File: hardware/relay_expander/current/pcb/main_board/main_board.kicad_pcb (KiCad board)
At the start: 2 copper layers, 100 x 85 mm, 101 parts, among them J1 Conn_01x07_Socket, J10 Screw_Terminal_01x02, J11 Screw_Terminal_01x02, J12 Screw_Terminal_01x02, J13 Screw_Terminal_01x02, J14 Screw_Terminal_01x02, J15 Screw_Terminal_01x02, J16 Conn_01x20_Socket, J2 Conn_01x07_Socket, J3 Screw_Terminal_01x02, J4 Screw_Terminal_01x02, J5 Screw_Terminal_01x02, J6 Screw_Terminal_01x02, J7 Screw_Terminal_01x02, J8 Screw_Terminal_01x03, J9 Screw_Terminal_01x02, K1 HF46F-12-HS1, K2 HF46F-12-HS1, K3 HF46F-12-HS1, K4 HF46F-12-HS1, K5 HF46F-12-HS1, K6 HF46F-12-HS1, K7 HF46F-12-HS1, K8 HF46F-12-HS1, Q1 BC548, Q2 BC548, Q3 BC548, Q4 BC548, Q5 BC548, Q6 BC548, Q7 BC548, Q8 BC548, SW1 SW_DIP_x03, U1 MCP23017x-x-SO, U2 TCMT4100, U3 TCMT4100, U4 TCMT4100, U5 TCMT4100

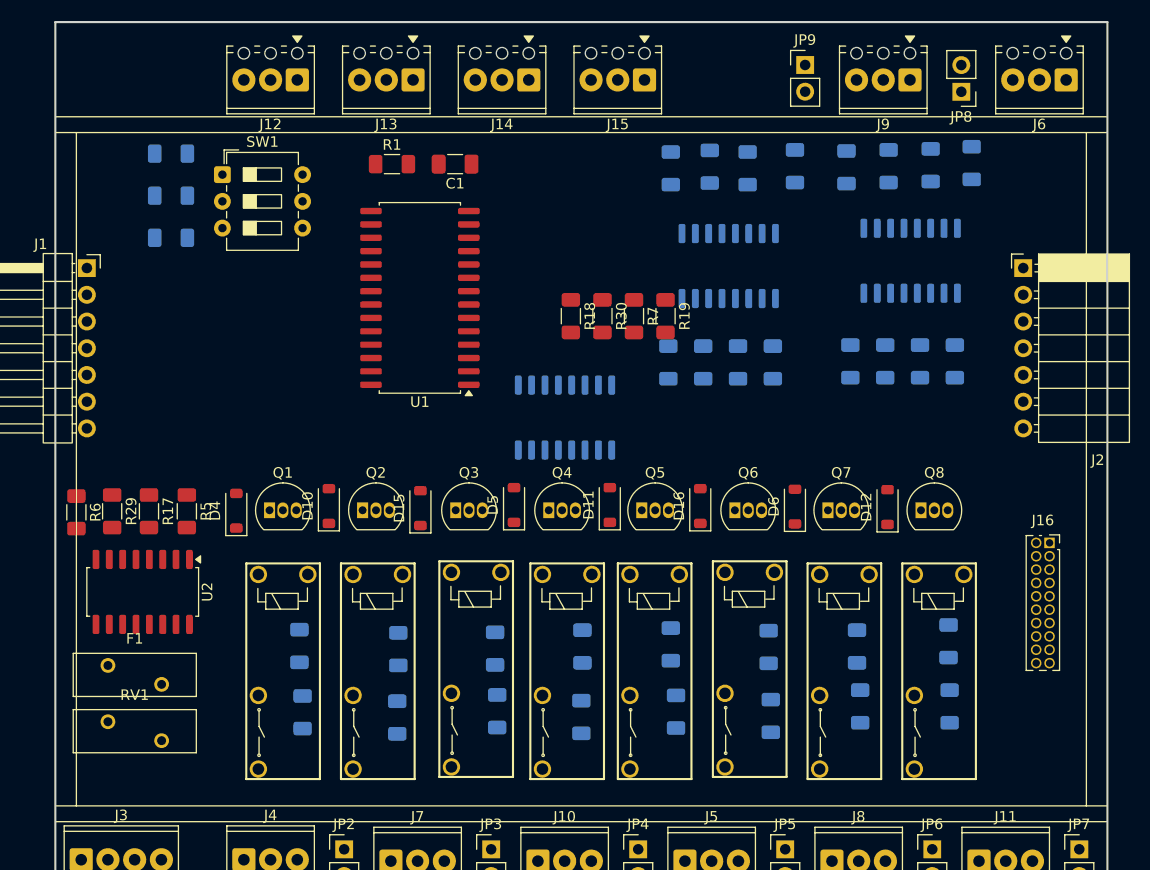
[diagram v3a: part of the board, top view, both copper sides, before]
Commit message: [FIX] placement of connector for UI panel
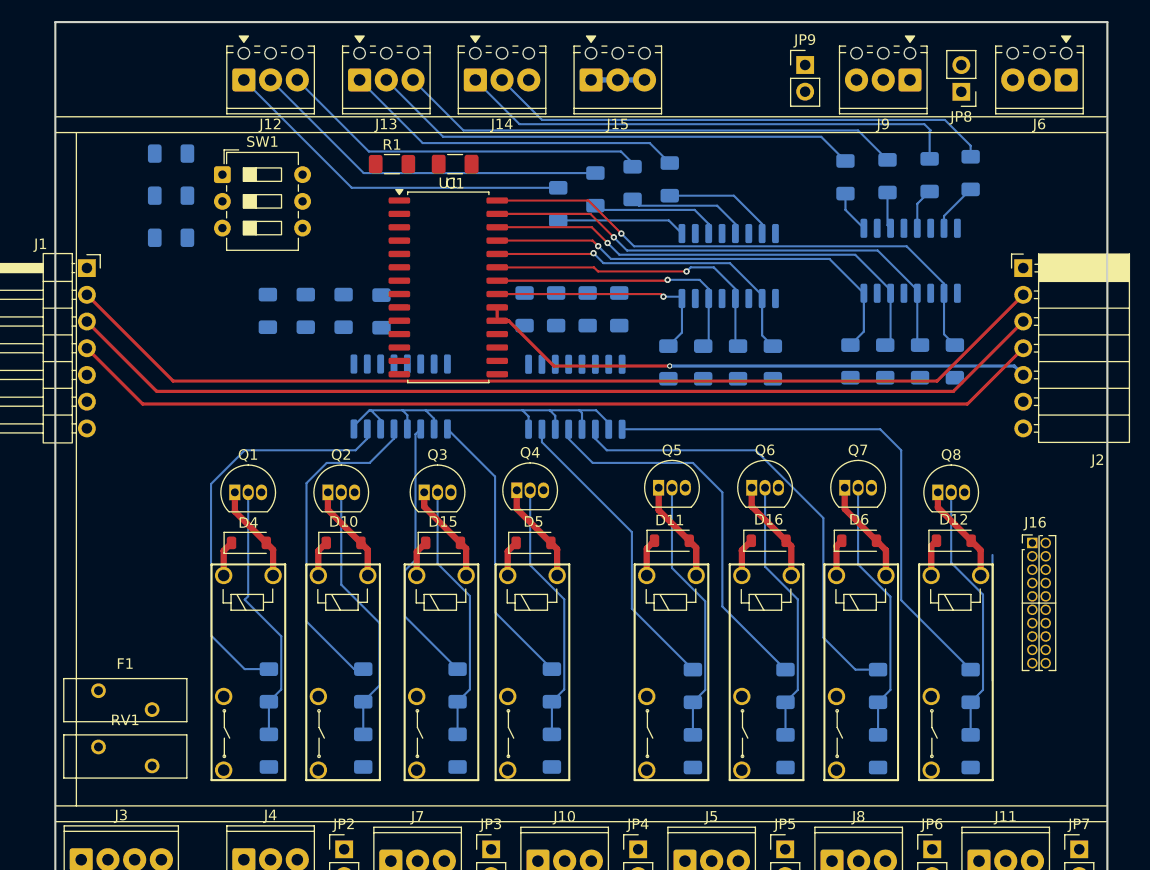
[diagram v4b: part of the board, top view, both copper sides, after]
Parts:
- J16: footprint Connector_PinSocket_1.27mm:PinSocket_2x10_P1.27mm_Vertical -> homeautomation_core:PinSocket_2x10_P1.27mm_Vertical
- R17, R18, R19, R29, R30, R5, R6, R7, U2: moved to B.Cu
- moved R6 34.7 mm to (116.0, 80.0)
- moved U2 30.8 mm to (117.8, 88.1)
- moved R29 29.1 mm to (112.4, 80.0)
- moved R17 24.2 mm to (108.8, 80.0)
- moved R5 20.5 mm to (105.2, 80.0)
- moved R40 12.0 mm to (143.4, 67.5)
- moved R37 11.2 mm to (132.8, 69.8)
- moved R38 11.1 mm to (136.3, 68.4)
- moved R39 11.0 mm to (139.9, 67.8)
- moved R28 10.7 mm to (172.0, 121.8)
- moved R26 10.4 mm to (145.6, 121.8)
- moved R12 10.4 mm to (105.3, 121.8)
- moved R34 10.3 mm to (123.2, 121.8)
- moved R14 10.3 mm to (132.2, 121.8)
- moved R24 10.2 mm to (114.3, 121.8)
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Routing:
- net +3V3: track 0.00 -> 95.8 mm
- net I2C_SDA: track 0.00 -> 94.5 mm
- net I2C_SCL: track 0.00 -> 93.4 mm
- net +12V: track 0.00 -> 71.5 mm
- net INT: track 0.00 -> 53.4 mm, vias 0 -> 1
- net /Digital_Inputs/In_7: track 0.00 -> 52.0 mm, vias 0 -> 1
- net Net-(R27-Pad1): track 0.00 -> 50.9 mm
- net /Digital_Inputs/In_6: track 0.00 -> 48.3 mm, vias 0 -> 1
- net Net-(J13-Pin_3): track 0.00 -> 48.2 mm
- net Net-(J14-Pin_2): track 0.00 -> 48.2 mm
- net Net-(J14-Pin_1): track 0.00 -> 48.0 mm
- net Net-(J13-Pin_2): track 0.00 -> 46.8 mm
- net /Digital_Inputs/In_5: track 0.00 -> 45.3 mm, vias 0 -> 1
- net Net-(R15-Pad1): track 0.00 -> 43.5 mm
- net /Digital_Inputs/In_4: track 0.00 -> 42.4 mm, vias 0 -> 1
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
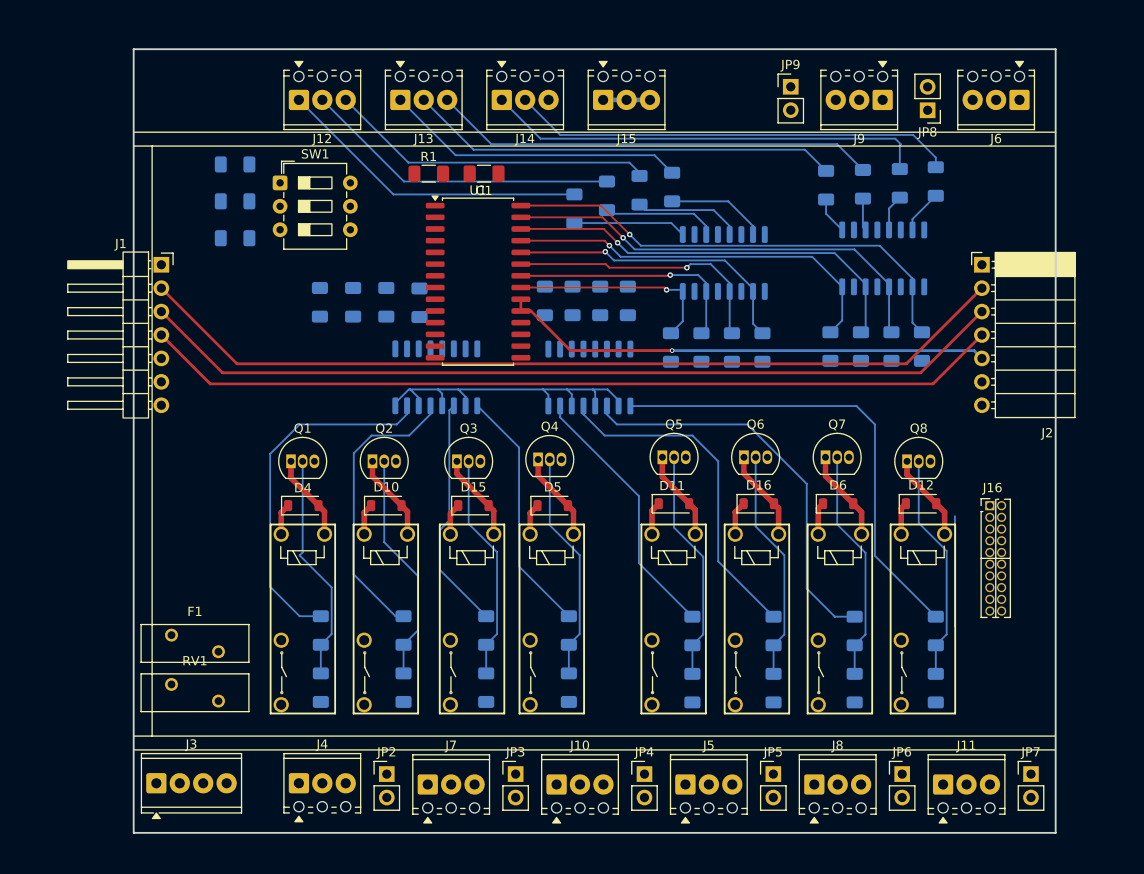
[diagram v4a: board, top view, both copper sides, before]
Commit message: [ADD] routing on main pcb board
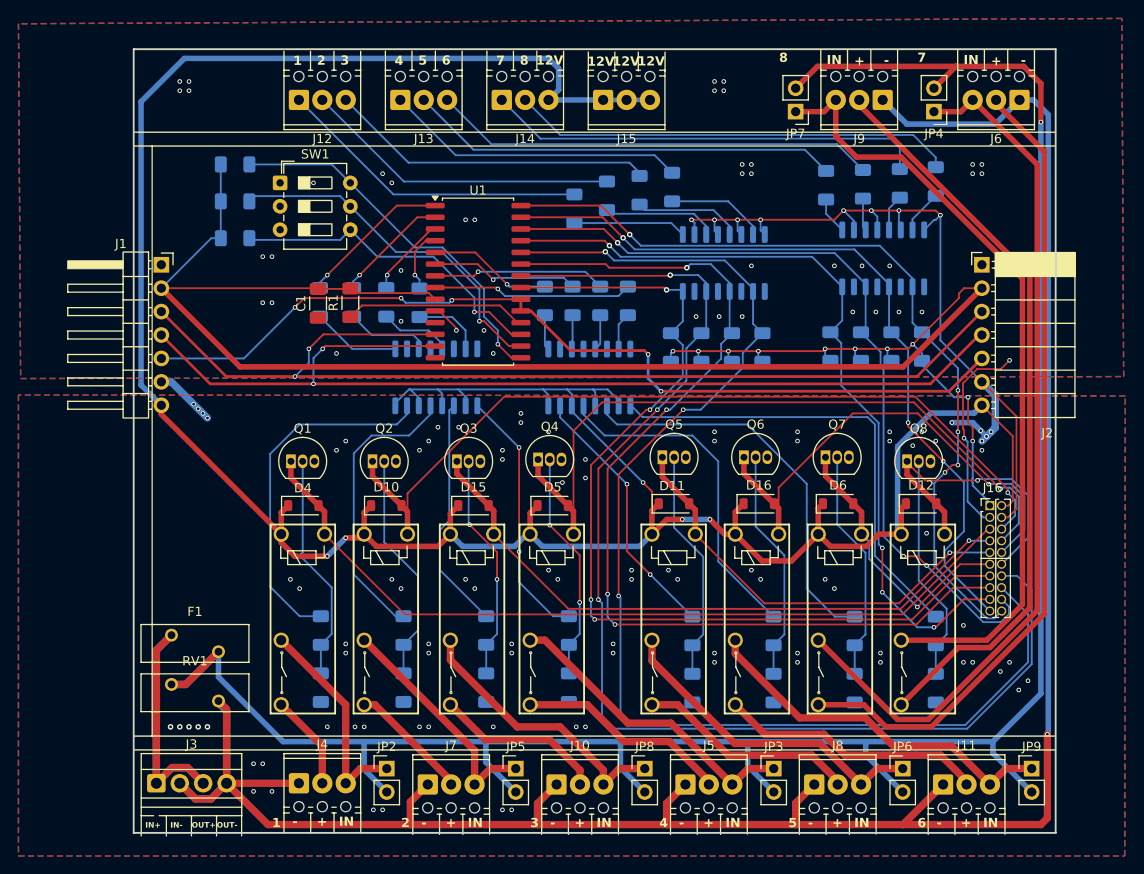
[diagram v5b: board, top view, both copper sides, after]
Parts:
- J10, J11, J4, J5, J6, J7, J8, J9: footprint TerminalBlock_Phoenix:TerminalBlock_Phoenix_MPT-0,5-3-2.54_1x03_P2.54mm_Horizontal -> homeautomation_core:TerminalBlock_Phoenix_MPT-0,5-3-2.54_1x03_P2.54mm_Horizontal_RELAY
- J3: footprint TerminalBlock_Phoenix:TerminalBlock_Phoenix_MPT-0,5-4-2.54_1x04_P2.54mm_Horizontal -> TerminalBlock:TerminalBlock_Xinya_XY308-2.54-4P_1x04_P2.54mm_Horizontal
- moved JP9 78.4 mm to (182.4, 130.5)
- moved JP4 78.4 mm to (171.8, 59.3), turned to 180 degrees
- moved JP8 77.7 mm to (140.4, 130.5), turned to 0 degrees
- moved JP7 76.2 mm to (156.8, 59.3), turned to 180 degrees
- moved JP3 28.0 mm to (154.4, 130.5)
- moved JP5 27.9 mm to (126.4, 130.5)
- moved C1 22.8 mm to (105.0, 80.1), turned to 90 degrees
- moved R1 16.4 mm to (108.5, 80.0), turned to 90 degrees
- moved JP6 0.60 mm to (168.4, 130.5)
- moved JP2 0.60 mm to (112.5, 130.5)
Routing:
- net L2: track 0.00 -> 254.6 mm, vias 0 -> 1
- net L1: track 0.00 -> 248.8 mm, vias 0 -> 1
- net +12V: track 71.5 -> 311.4 mm, vias 0 -> 5
- net +3V3: track 95.8 -> 211.2 mm, vias 0 -> 10
- net /Digital_Inputs/In_1: track 26.1 -> 134.4 mm, vias 1 -> 3
- net /Digital_Inputs/In_3: track 32.1 -> 137.8 mm, vias 1 -> 3
- net GND_2: track 0.00 -> 100.1 mm, vias 0 -> 100
- net Net-(J6-Pin_3): track 0.00 -> 95.2 mm
- net Net-(J6-Pin_2): track 0.00 -> 88.5 mm
- net Net-(J9-Pin_3): track 0.00 -> 85.6 mm
- net /Relays/LED_RELAY_2: track 9.47 -> 92.8 mm, vias 0 -> 1
- net Net-(J9-Pin_2): track 0.00 -> 81.0 mm
- net /Digital_Inputs/In_0: track 22.8 -> 103.7 mm, vias 1 -> 4
- net /Digital_Inputs/In_2: track 29.4 -> 109.4 mm, vias 1 -> 4
- net /Relays/LED_RELAY_1: track 9.41 -> 89.0 mm
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- added copper zone on B.Cu, net GND
- added copper zone on F.Cu, net GND
- added copper zone on B.Cu, net GND_2
- added copper zone on F.Cu, net GND_2
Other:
- board text added: "1"
- board text added: "2"
- board text added: "3"
- board text added: "4"
- board text added: "5"
- board text added: "6"
- board text added: "7"
- board text added: "8"
- board text added: "IN-"
- board text added: "OUT+"
- board text added: "OUT-"

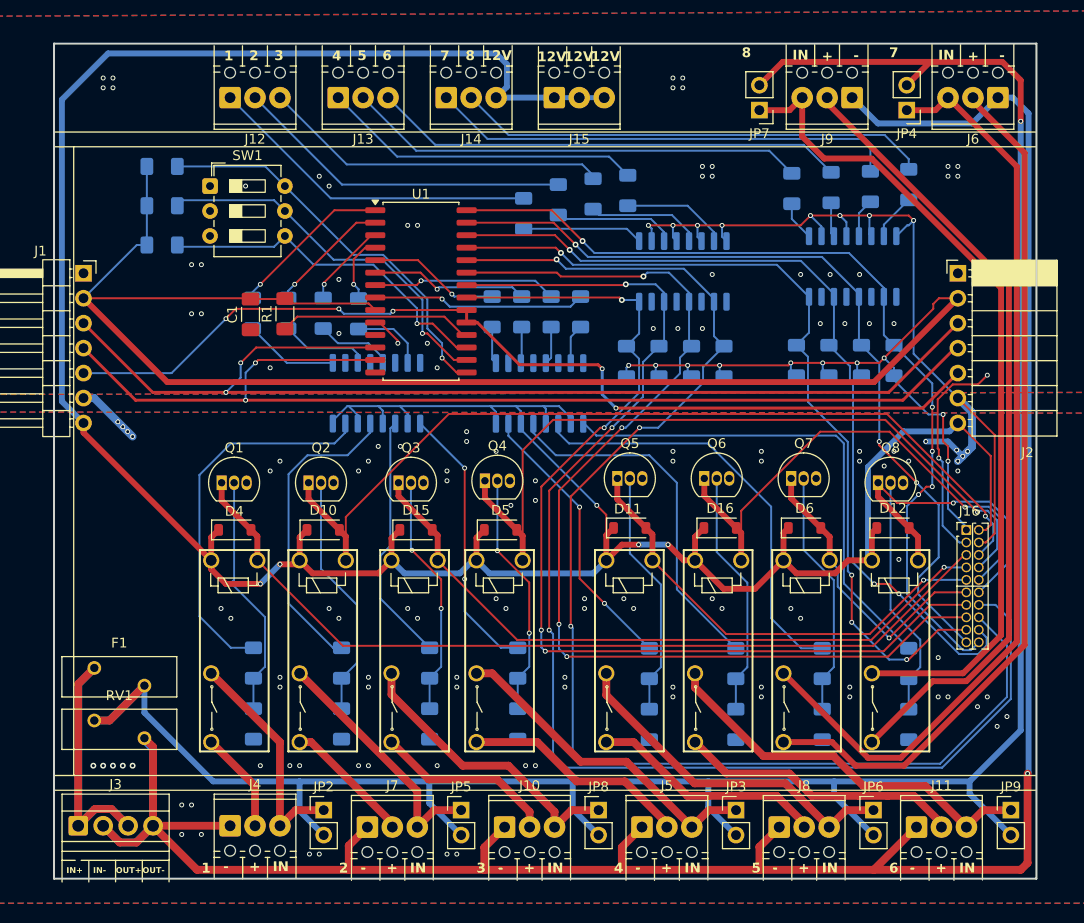
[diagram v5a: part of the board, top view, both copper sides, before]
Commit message: [FIX] add 12V trace for expanders and generate gerber for all relays related boards
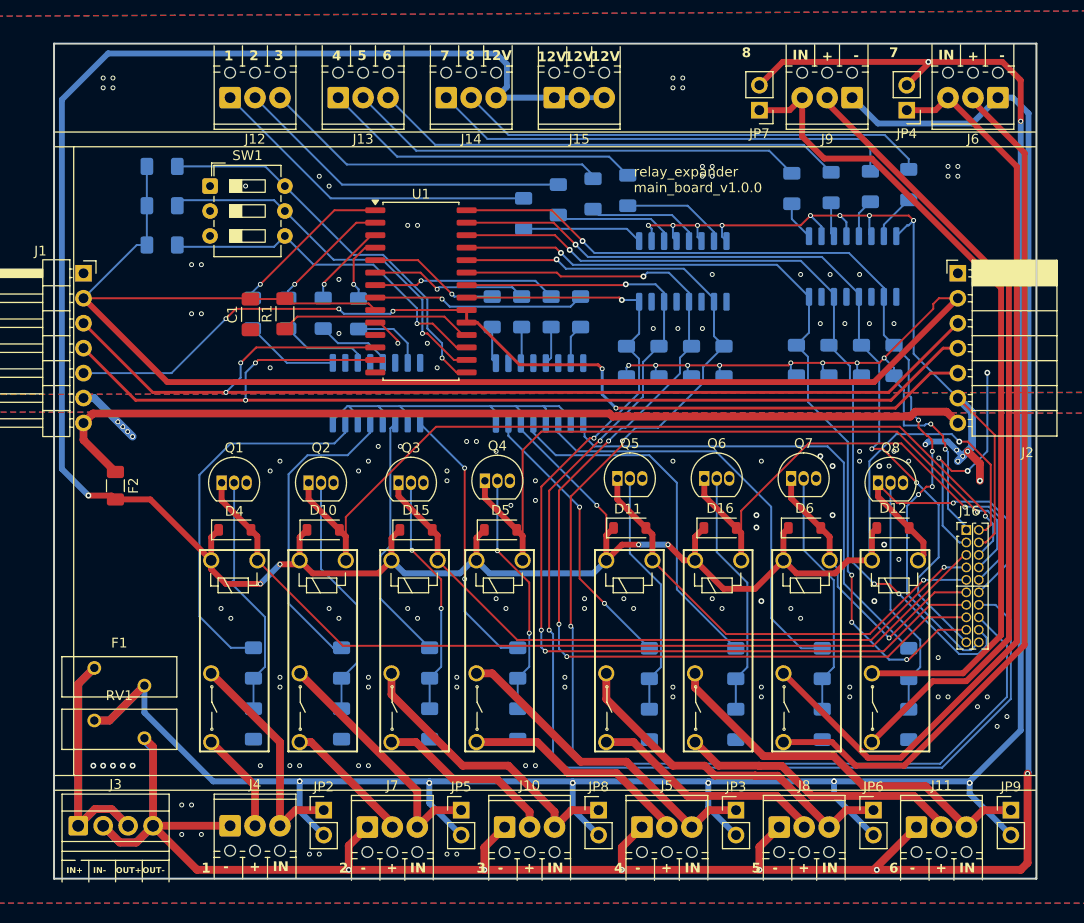
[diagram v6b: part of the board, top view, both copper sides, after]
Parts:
- added F2: 0.5A, Fuse:Fuse_1206_3216Metric, F.Cu at (91.2, 97.5)
- J10, J11, J12, J13, J14, J15, J4, J5, J6, J7, J9: value Screw_Terminal_01x02 -> Screw_Terminal_01x03
- J3: value Screw_Terminal_01x02 -> Screw_Terminal_01x04
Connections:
- J1 pad 7: +12V -> +12V_BUS
- J2 pad 7: +12V -> +12V_BUS
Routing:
- net +12V_BUS: track 0.00 -> 95.8 mm
- net GND_2: track 100.1 -> 103.8 mm, vias 100 -> 106
- net GND: track 25.6 -> 27.8 mm, vias 44 -> 45
- net +12V: track 311.4 -> 313.6 mm, vias 5 -> 7
- net /Digital_Inputs/In_6: track 84.7 -> 85.9 mm
- net /Relays/LED_RELAY_2: track 92.8 -> 91.7 mm
- net /Relays/LED_RELAY_6: track 55.8 -> 54.8 mm
- net /Relays/LED_RELAY_4: track 80.4 -> 79.4 mm
- net +3V3: track 211.2 -> 212.2 mm
- net L2: vias 1 -> 6
- net L1: vias 1 -> 8
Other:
- board text added: "relay_expander main_board_v1.0.0"
